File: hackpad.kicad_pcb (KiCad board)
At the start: 2 copper layers, 83.3 x 107.2 mm, 33 parts, among them SW1 SW_Push, SW10 SW_Push, SW11 SW_Push, SW12 SW_Push, SW13 SW_Push, SW14 SW_Push, SW15 SW_Push, SW16 SW_Push, SW2 SW_Push, SW3 SW_Push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

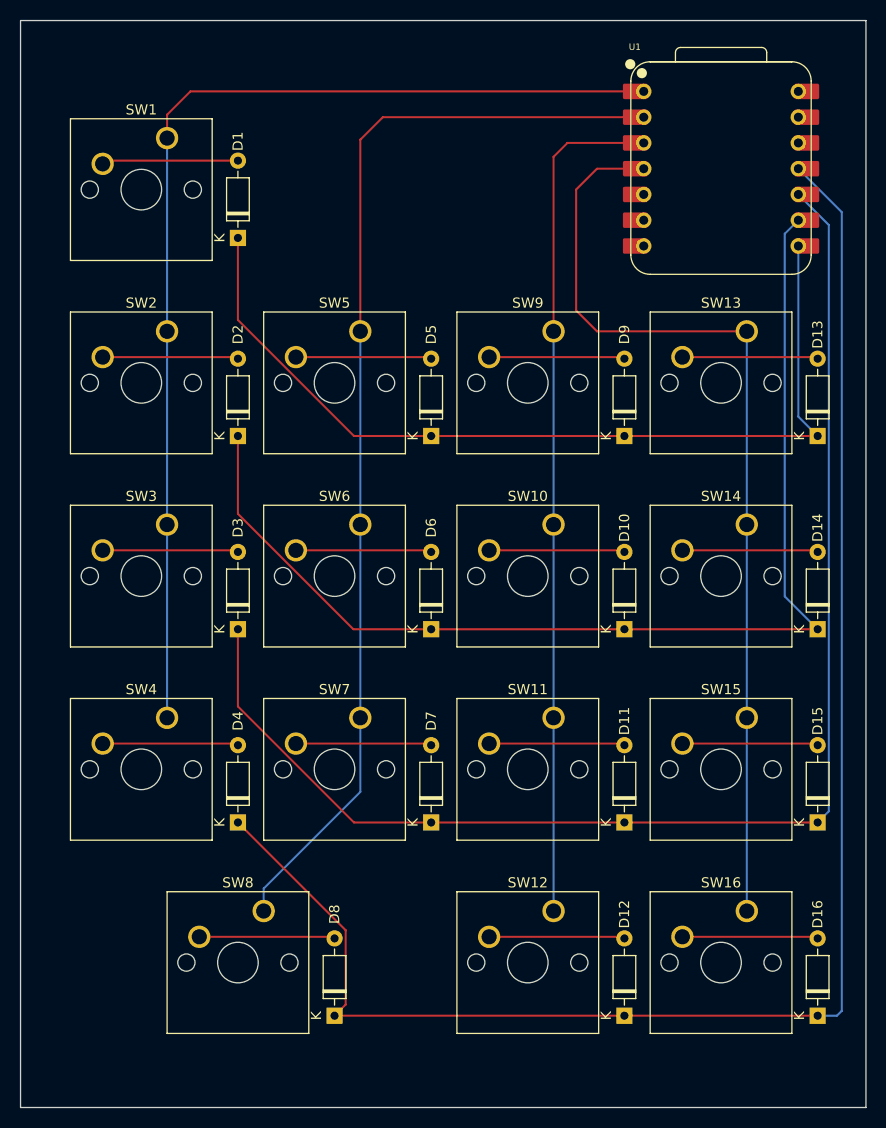
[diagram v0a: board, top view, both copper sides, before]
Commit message: Added branding to PCB and adjusted MC to spec
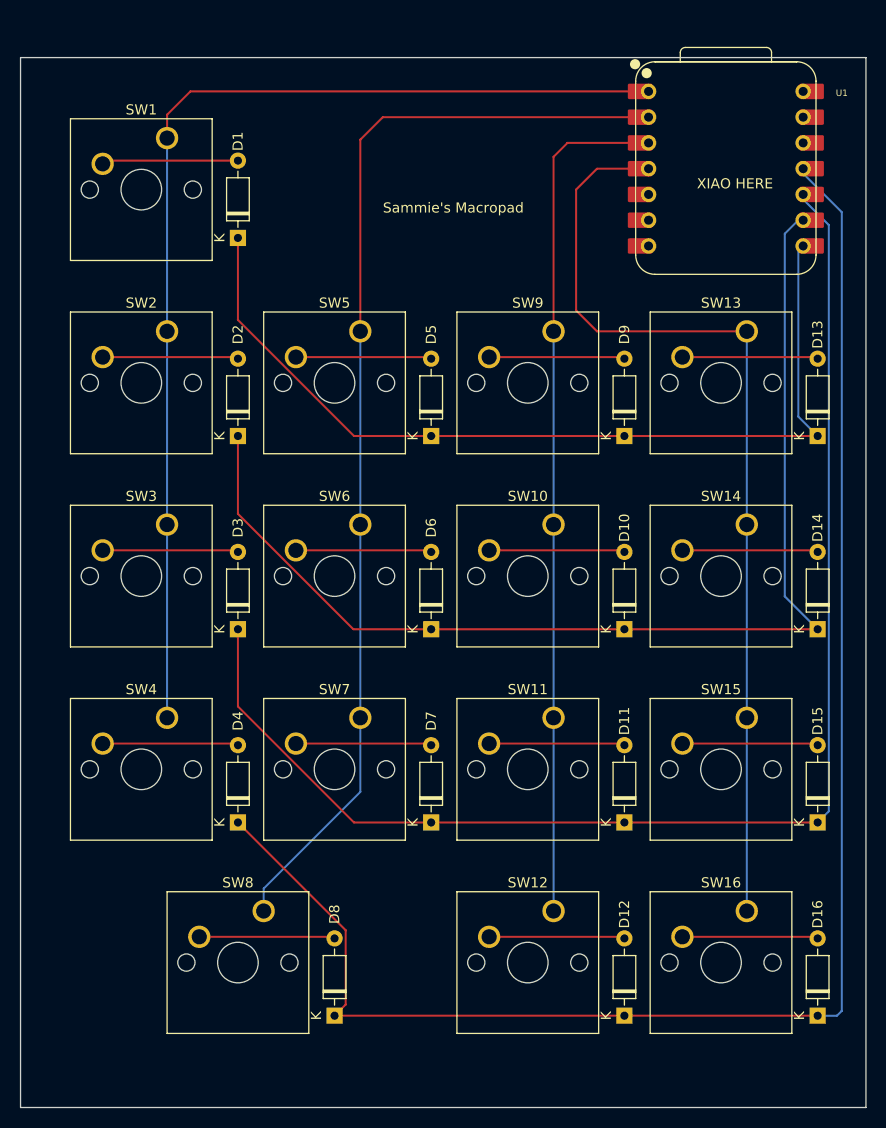
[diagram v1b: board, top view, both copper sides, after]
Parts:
- moved U1 0.48 mm to (95.7, 43.2)
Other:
- board size 83.3 x 107.2 mm -> 83.3 x 103.5 mm
- board text added: "Sammie's Macropad"
- board text added: "XIAO HERE"
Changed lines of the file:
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@@
 	(footprint "OPL:XIAO-RP2040-DIP"
 		(layer "F.Cu")
-		(at 95.25 43.18)
+		(at 95.72625 43.18)
 		(property "Reference" "U1"
-			(at -8.5 -12 0)
+			(at 11.43 -7.46125 0)
 			(unlocked yes)
 			(layer "F.SilkS")
@@
 	)
 	(gr_rect
-		(start 26.19375 28.575)
+		(start 26.19375 32.22625)
 		(end 109.5375 135.73125)
 		(stroke
@@
 		(layer "Edge.Cuts")
 	)
+	(gr_text "Sammie's Macropad"
+		(at 61.9125 47.625 0)
+		(layer "F.SilkS")
+		(effects
+			(font
+				(size 1 1)
+				(thickness 0.15)
+			)
+			(justify left bottom)
+		)
+	)
+	(gr_text "XIAO HERE"
+		(at 92.86875 45.24375 0)
+		(layer "F.SilkS")
+		(effects
+			(font
+				(size 1 1)
+				(thickness 0.15)
+			)
+			(justify left bottom)
+		)
+	)
 	(segment

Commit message: Finished Top plate and changed case. Added 3d model of PCB and other relevant components.
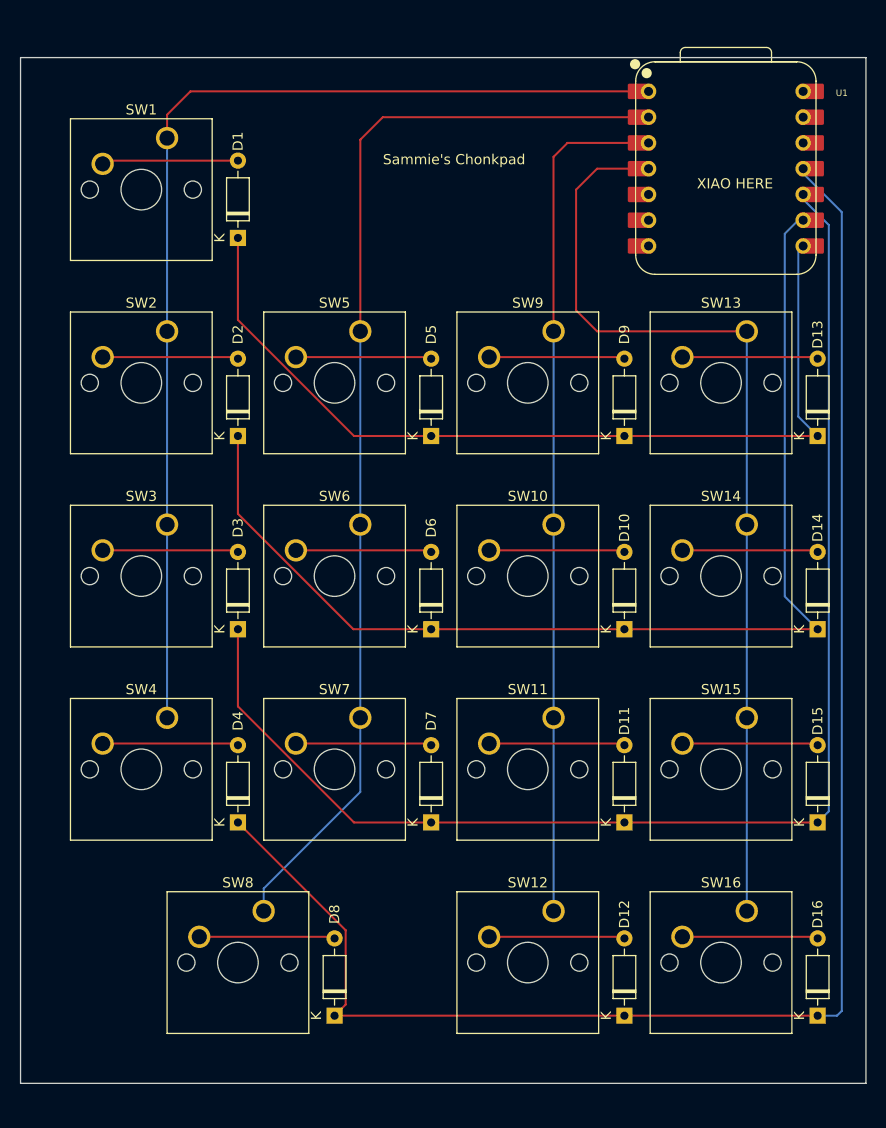
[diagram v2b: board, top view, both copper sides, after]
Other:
- board size 83.3 x 103.5 mm -> 83.3 x 101.1 mm
- board text added: "Sammie's Chonkpad"
- board text removed: "Sammie's Macropad"
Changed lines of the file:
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@@
+			)
+		)
+		(model "${KIPRJMOD}/Seeed Studio XIAO RP2040 v26.step"
+			(offset
+				(xyz 0 0 0)
+			)
+			(scale
+				(xyz 1 1 1)
+			)
+			(rotate
+				(xyz 0 0 0)
 			)
 		)
@@
 	(gr_rect
 		(start 26.19375 32.22625)
-		(end 109.5375 135.73125)
+		(end 109.5375 133.35)
 		(stroke
 			(width 0.05)
@@
 		(layer "Edge.Cuts")
 	)
-	(gr_text "Sammie's Macropad"
-		(at 61.9125 47.625 0)
+	(gr_text "Sammie's Chonkpad"
+		(at 61.9125 42.8625 0)
 		(layer "F.SilkS")
 		(effects
